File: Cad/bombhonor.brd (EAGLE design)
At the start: 66 x 62.8 mm, 75 parts, among them CN1 HEADER4X1_2MM_SMD, CN2 TR1-01, U1 STM32F030F4

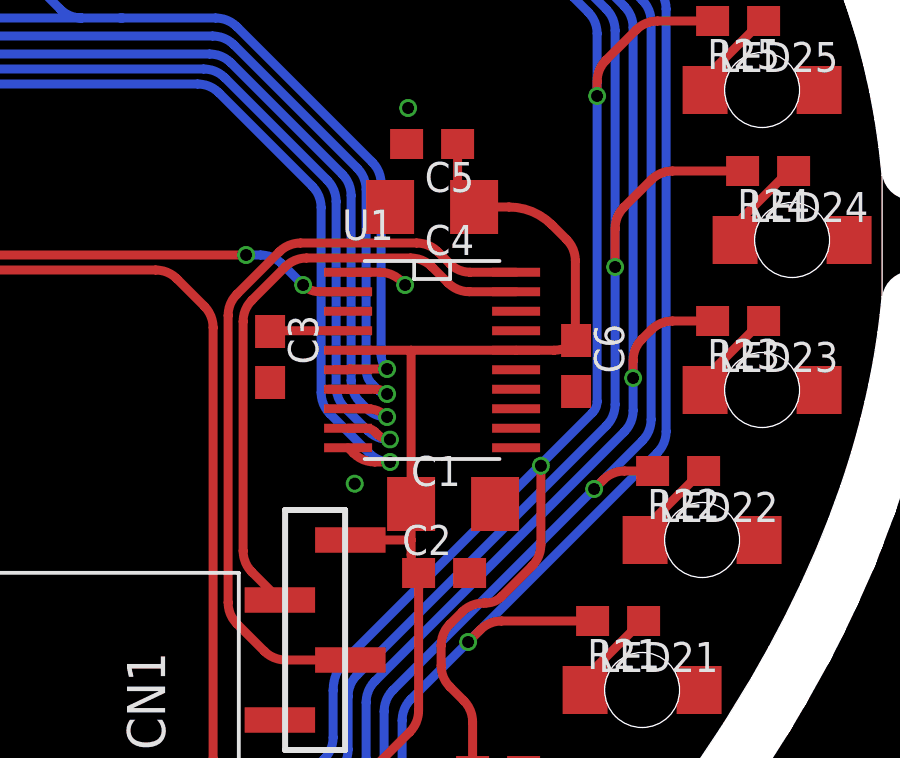
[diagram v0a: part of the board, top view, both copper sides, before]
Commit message: Terminata la BOM, da calcolare la spesa totale
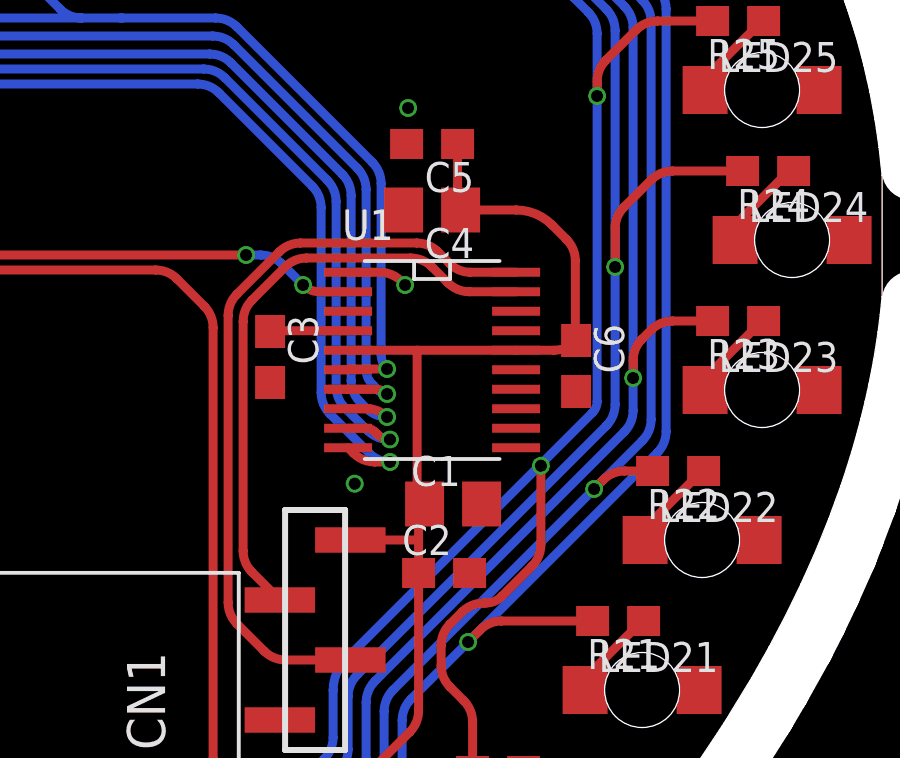
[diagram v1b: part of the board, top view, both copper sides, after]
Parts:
- C1, C4: device AlmaPASS:1206[3216] -> AlmaPASS:0805[2012]
- moved C4 0.10 mm to (17.0, 11.0)
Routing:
- net +3V3: track 87.2 -> 87.9 mm

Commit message: Messi a posto nomi e dettagli. La bom costa 3.85€
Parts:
- moved C5 4.61 mm to (21.0, 10.9), turned to 0 degrees
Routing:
- net +3V3: track 87.9 -> 86.1 mm
- net LED2: track 198.4 -> 197.7 mm
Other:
- board text added: "12.09.2020"

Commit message: Messe a posto le piste
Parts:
- added U$3, U$4, U$5: (no value), AlmaPANEL:FIDUCIAL_1MM+2MM+CREAM
- moved C3 0.60 mm to (12.2, 6.10)
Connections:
- net LED1: now also U1.10; no longer U1.6
- net LED2: now also U1.9; no longer U1.7
- net LED4: now also U1.7; no longer U1.9
- net LED5: now also U1.6; no longer U1.10
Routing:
- net ON: track 32.5 -> 64.4 mm, vias 2 -> 0
- net LED1: track 185.6 -> 194.5 mm
- net LED5: track 206.5 -> 202.6 mm
- net LED2: track 197.7 -> 201.4 mm
- net LED4: track 202.4 -> 205.0 mm
- net LED3: track 195.9 -> 197.2 mm
- net +3V3: track 86.1 -> 85.3 mm
- net NRST: track 2.61 -> 2.01 mm
- net GND: vias 6 -> 7
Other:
- board size 66 x 62.8 mm -> 80 x 67.4 mm
- board text removed: "C:/Users/lori91et3/Desktop/b.bmp"

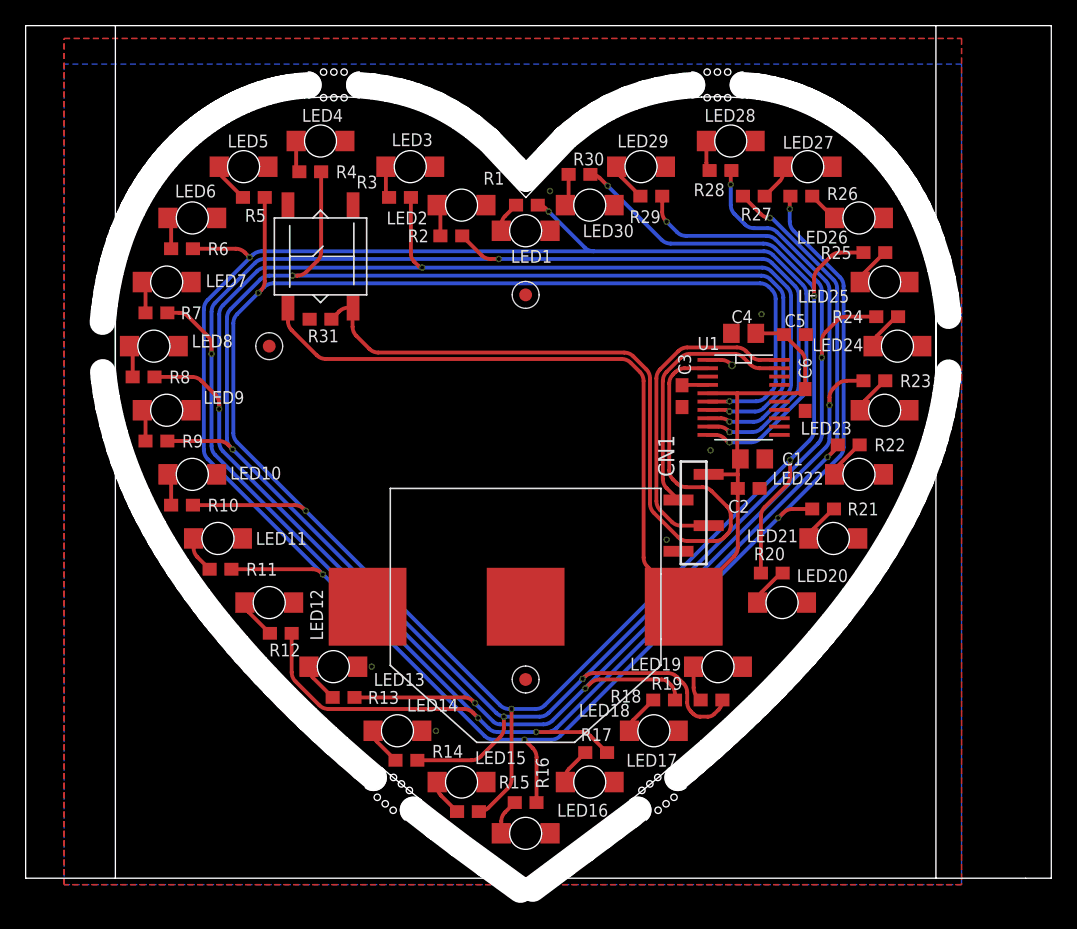
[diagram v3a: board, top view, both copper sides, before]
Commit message: Aggiunto firmware base che si illumina. Messa a posto la bom e scritto commenti con partno sullo schematico
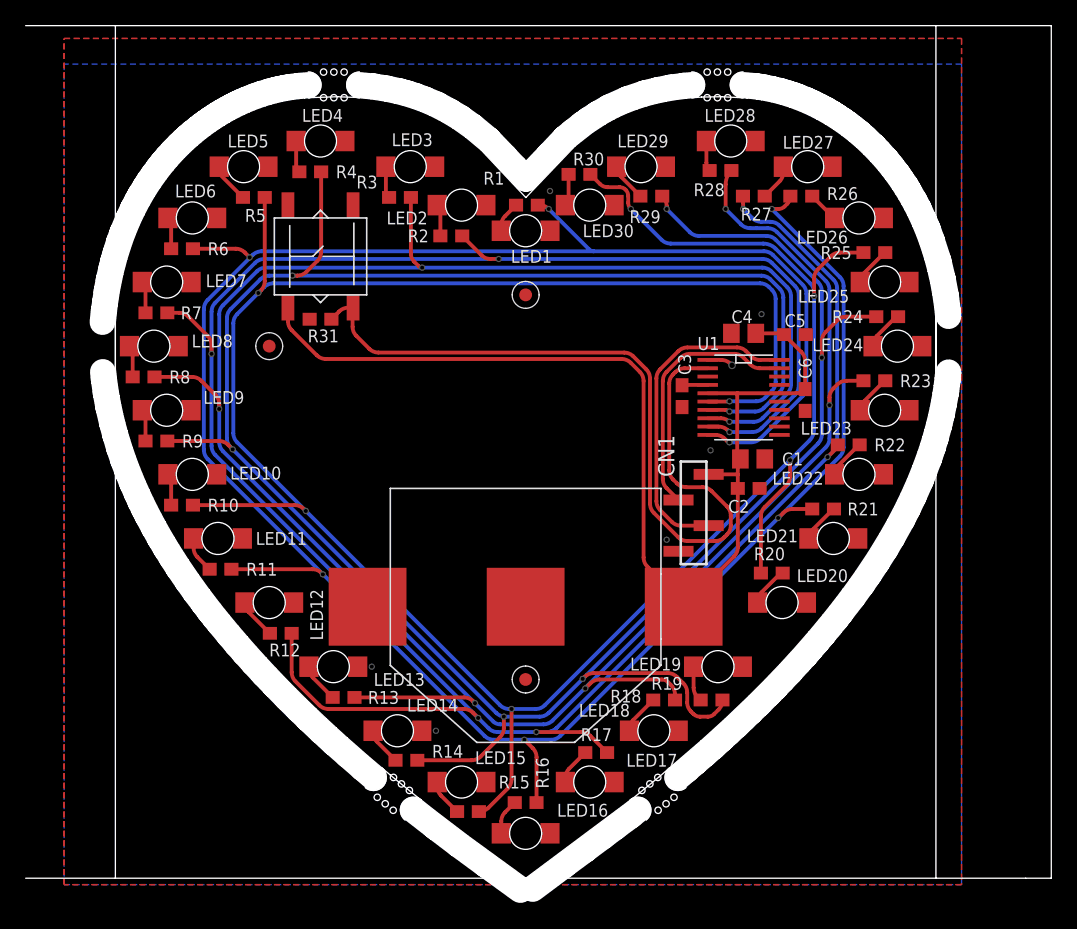
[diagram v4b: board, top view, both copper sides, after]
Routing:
- net LED1: track 194.5 -> 196.2 mm
- net LED2: track 201.4 -> 202.3 mm
- net LED5: track 202.6 -> 203.2 mm
- net LED4: track 205.0 -> 204.4 mm

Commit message: Messi i testpad sul PCB invece che il connettore Creato il primo supporto da provare a stampare
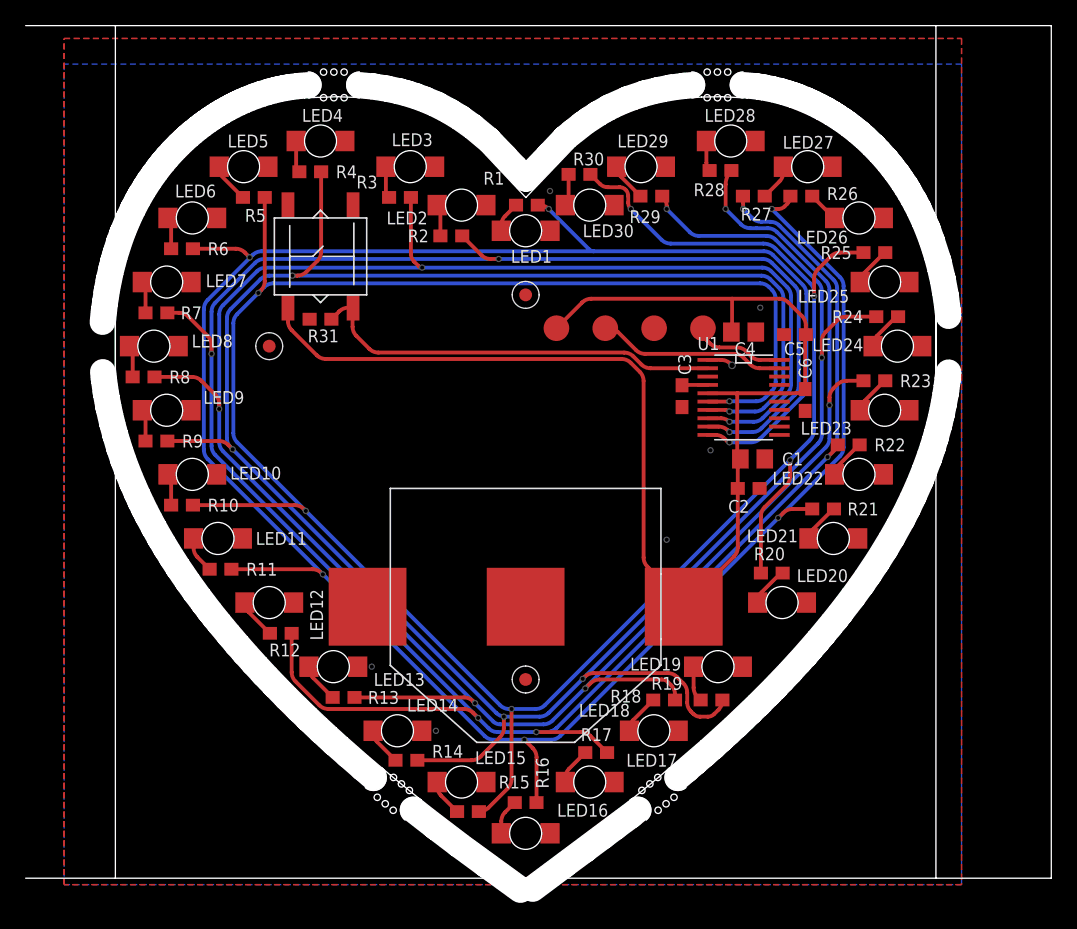
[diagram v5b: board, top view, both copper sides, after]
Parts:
- removed CN1: HEADER4X1_2MM_SMD, AlmaCONN:HEADER4X1_2MM_SMD
- added TP1, TP2, TP3, TP4: TESTPAD2MM, AlmaCONN:TP-2MM
- U1: value STM32F030F4 -> STM32L011F4P6
- moved C4 0.10 mm to (17.0, 11.1), turned to 0 degrees
- turned C5 to 180 degrees
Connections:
- net +3V3: now also TP1.TP; no longer CN1.4
- net GND: now also TP3.TP; no longer CN1.1
- net SWCLK: now also TP4.TP; no longer CN1.2
- net SWDIO: now also TP2.TP; no longer CN1.3
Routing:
- net ON: track 64.4 -> 32.5 mm
- net +3V3: track 85.3 -> 104.8 mm
- net SWCLK: track 25.6 -> 7.12 mm
- net SWDIO: track 20.2 -> 14.6 mm
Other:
- outline, holes or cut-outs redrawn

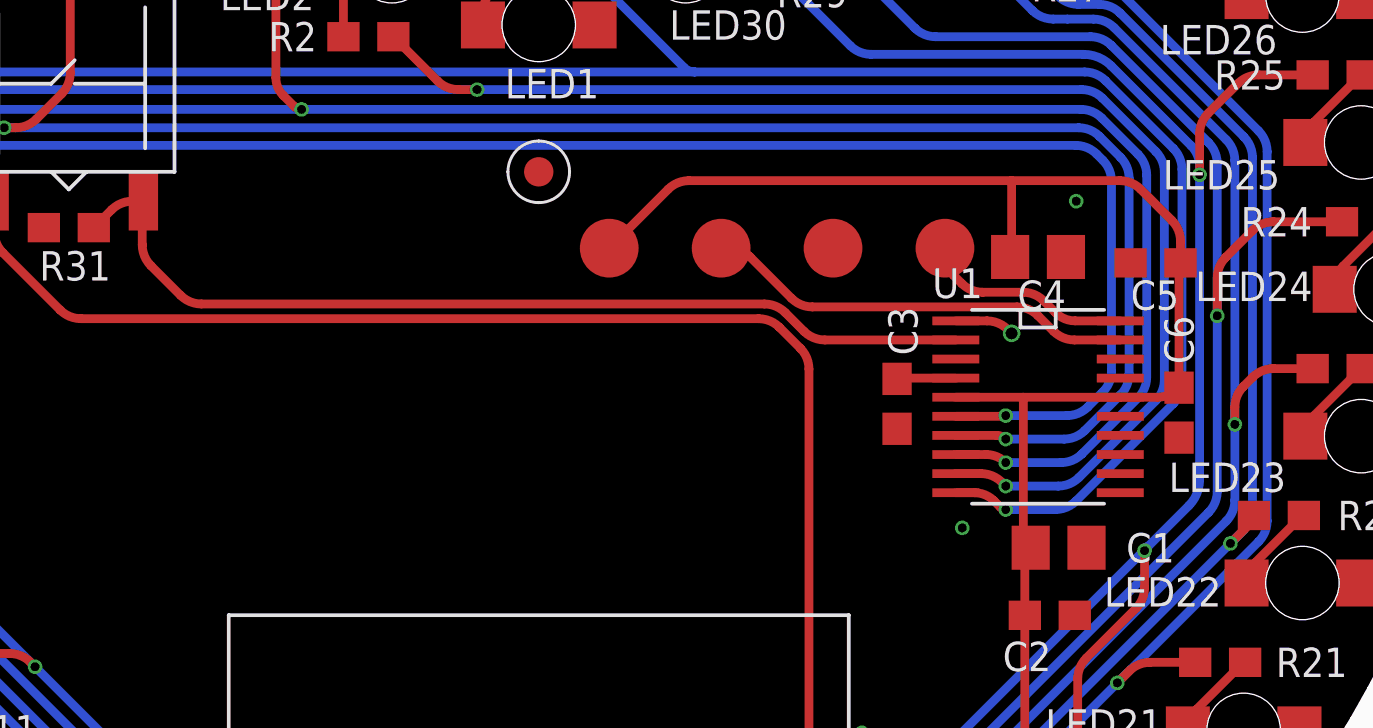
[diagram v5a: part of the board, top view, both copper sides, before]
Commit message: Modificata scheda per avere i pin a posto con l'STM32L011. Creata fantasia su vecchia scheda. Aggiunto codice nuovo micro
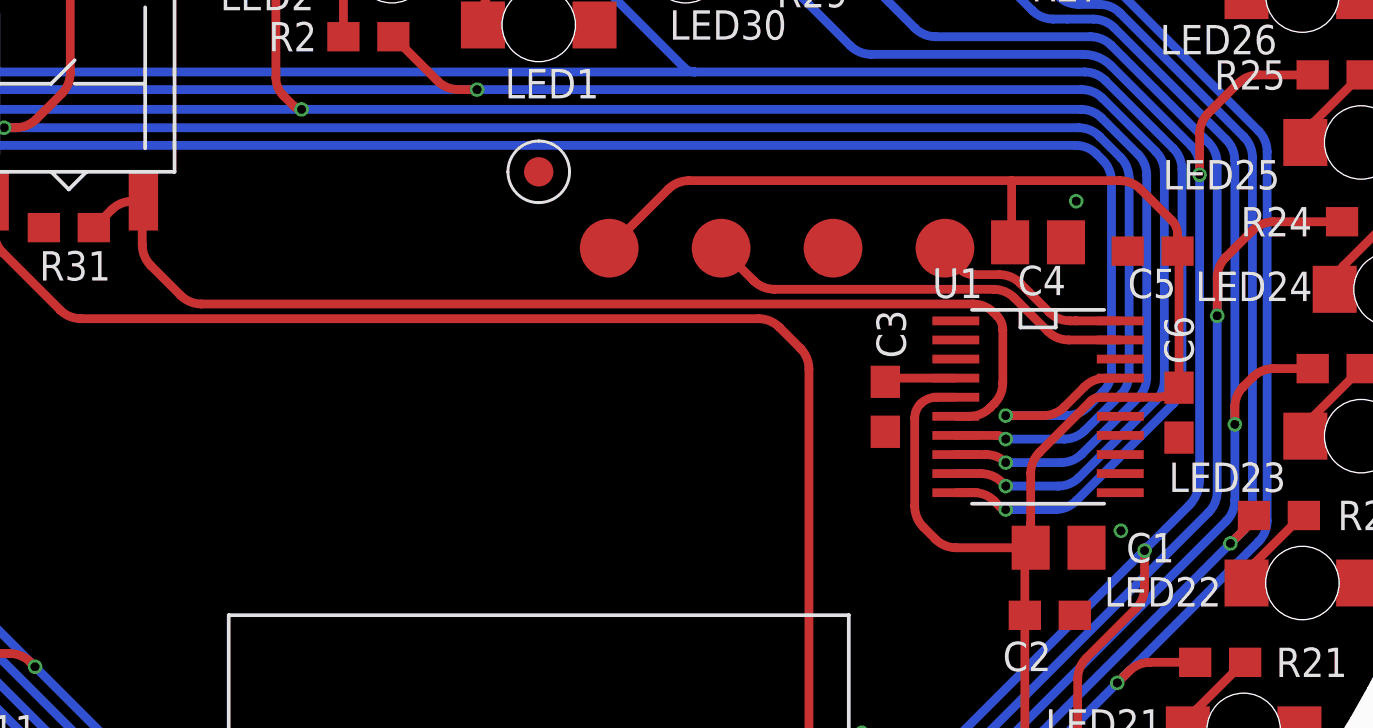
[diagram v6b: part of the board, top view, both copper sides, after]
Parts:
- moved C4 0.50 mm to (17.0, 11.6)
- moved C5 0.41 mm to (20.9, 11.3)
- moved C3 0.41 mm to (11.8, 6.00)
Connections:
- net LED5: now also U1.17; no longer U1.6
- net ON: now also U1.6; no longer U1.2
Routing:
- net +3V3: track 104.8 -> 110.5 mm
- net ON: track 32.5 -> 38.2 mm
- net LED5: track 203.2 -> 205.8 mm
- net GND: track 2.01 -> 0.00 mm, vias 7 -> 6

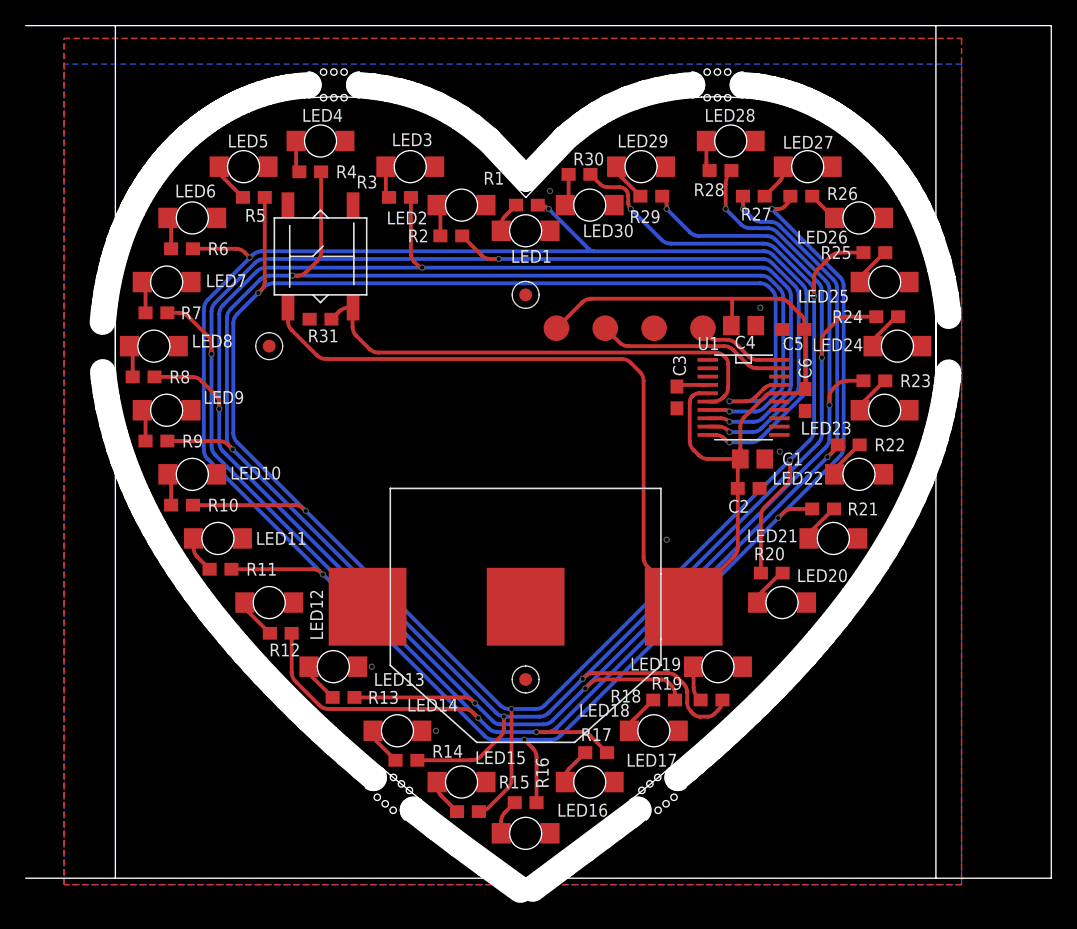
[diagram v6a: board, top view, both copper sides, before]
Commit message: Iniziata a mettere aposto la scheda. cambiato pulsante. il reset non ci sta
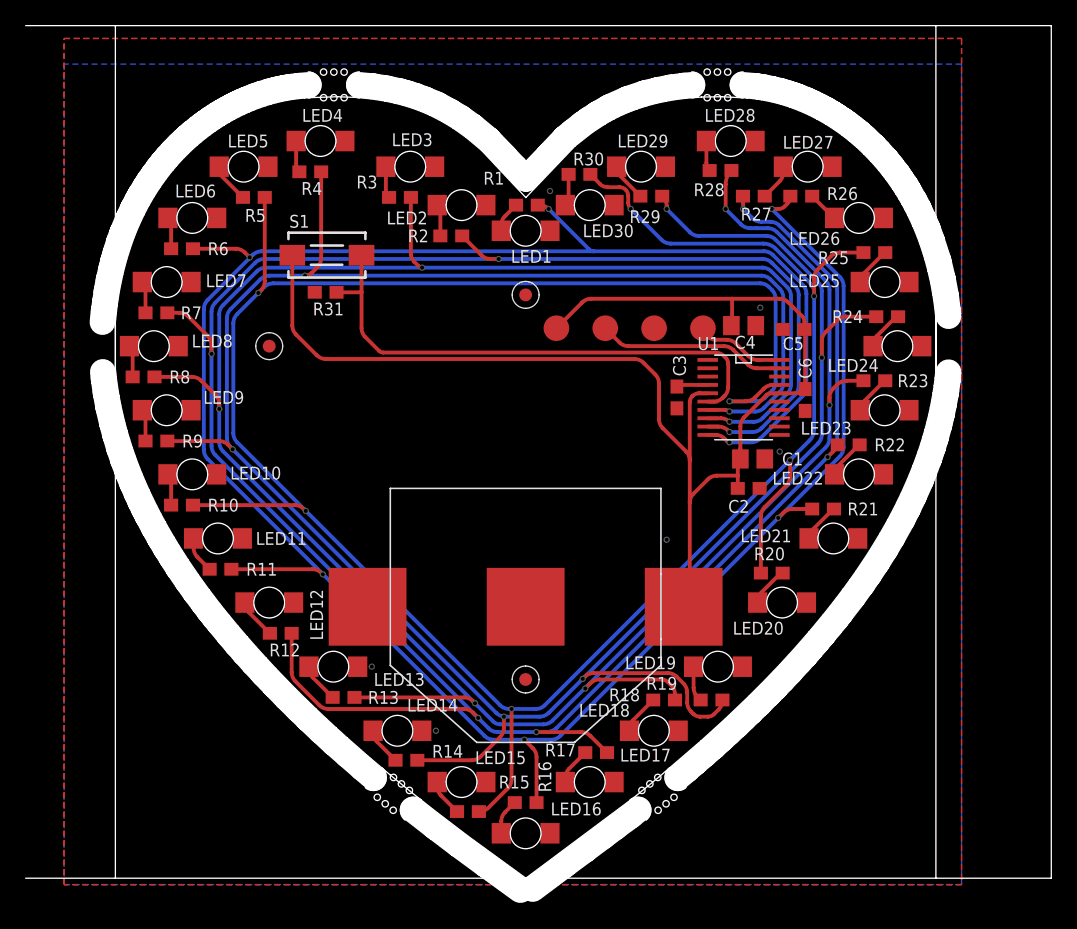
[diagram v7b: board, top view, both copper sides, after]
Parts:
- removed CN2: TR1-01, cesso:MAROGNATA
- added S1: DTSM-3, switch-tact:DTSM-3
- moved R31 2.14 mm to (-15.6, 14.2)
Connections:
- net +3V3: now also S1.1; no longer CN2.1
- net ON: now also S1.2; no longer CN2.3
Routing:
- net +3V3: track 110.5 -> 106.2 mm
- net ON: track 38.2 -> 41.6 mm
- net LED4: track 204.4 -> 203.7 mm

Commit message: Aggiustata scritta e messi a posto un po' di pistolini
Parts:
- added U$6: (no value), cesso:SCRITTA2
- moved R30 6.25 mm to (8.20, 18.6)
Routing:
- net N$30: track 2.45 -> 5.76 mm
- net LED5: track 205.8 -> 202.9 mm
- net GND: track 0.00 -> 2.24 mm, vias 6 -> 8
- net +3V3: track 106.2 -> 105.4 mm
- net LED2: track 202.3 -> 201.5 mm
